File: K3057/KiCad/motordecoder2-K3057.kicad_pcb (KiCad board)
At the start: 2 copper layers, 69 x 14 mm, 85 parts, among them J11 PAD, J12 PAD, J14 PAD, J16 PAD, J18 PAD, J19 PAD, P10 PAD, P11 PAD, P21 PAD, P22 PAD, P23 PAD, P24 PAD, P25 PAD, P26 PAD, P27 PAD, P28 PAD, P29 PAD, P31 PAD, P7 PAD, P8 PAD, P9 PROG, Q1 DMG6601LVT, Q11 SSM6N7002BFE, Q12 SSM6N7002BFE, Q13 SSM6N7002BFE, Q14 SSM6N7002BFE, Q15 SSM3K7002BFU, Q2 DMG6601LVT, Q21 PMBT3906VS, Q22 SSM6N7002BFE, Q3 PMBT3904VS, Q5 2SC4116, Q6 PMBT3906VS, Q8 PMBT3904VS, U2 ATtiny1606-M

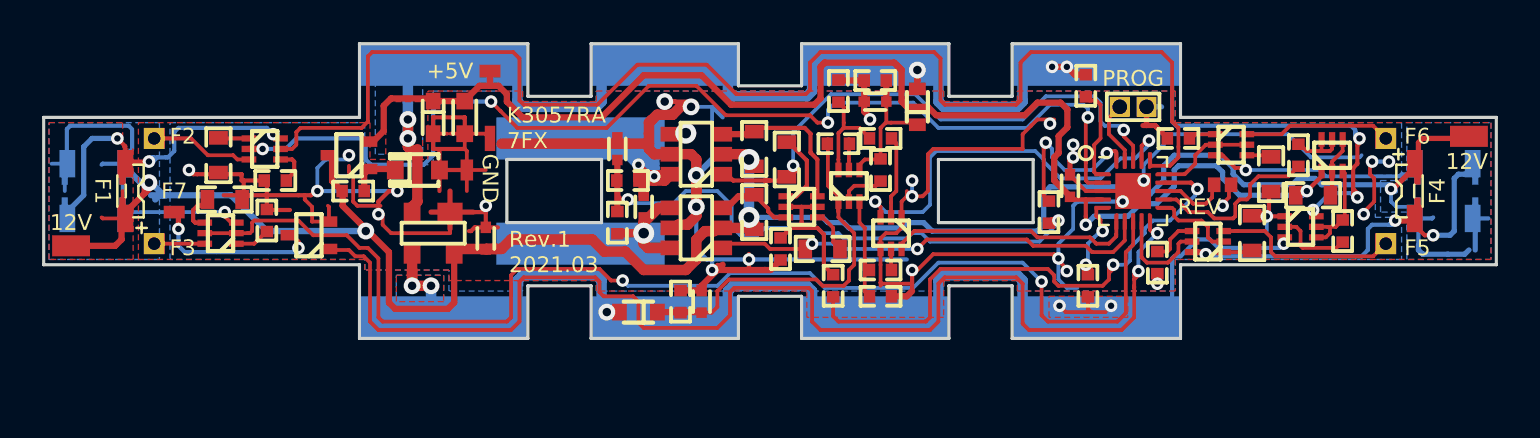
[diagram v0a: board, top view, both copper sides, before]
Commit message: 回路の問題点を修正 (K3066: Rev3 / それ以外: Rev2)
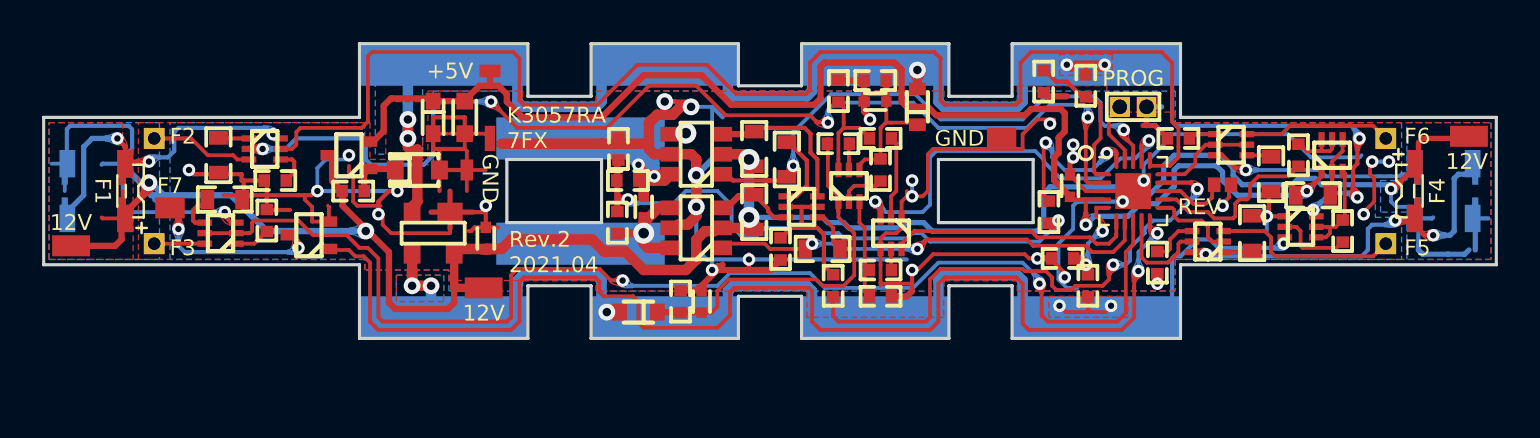
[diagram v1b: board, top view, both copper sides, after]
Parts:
- removed C6: 104, footprint:C_1005_v2
- added J13: PAD, footprint:PAD_1.0x1.8_SMD, F.Cu at (120.4, 91.6)
- added P12: PAD, footprint:PAD_1.0x1.4_SMD, F.Cu at (145.0, 84.5)
- added R16: 103, footprint:R_1005, F.Cu at (126.8, 85.0)
- added R17: 104, footprint:R_1005, F.Cu at (147.0, 81.8)
- added R18: 104, footprint:R_1005, F.Cu at (147.9, 90.2)
- C7: value 104 -> 182
- J19: footprint footprint:PAD_0.6x1.0_SMD -> footprint:PAD_1.0x1.4_SMD
- R23, R24, R25, R26: value 102 -> 472
- moved J19 0.28 mm to (105.5, 87.8)
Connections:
- net Func8 renamed DIR_JP
- Q11 pad 5: Func6 -> Func2
- Q12 pad 2: Func2 -> Func4
- Q12 pad 5: Func3 -> Func5
- Q13 pad 2: Func4 -> Func3
- Q13 pad 5: Func4 -> Func3
- Q14 pad 2: Func5 -> Func6
- Q14 pad 5: Func5 -> Func6
- U2 pad 11: Func2 -> Func4
- U2 pad 15: Func5 -> Func6
- U2 pad 16: Func6 -> Func2
- U2 pad 8: Func4 -> Func3
- U2 pad 9: Func3 -> Func5
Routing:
- net Func2: track 3.98 -> 62.9 mm
- net Func6: track 62.9 -> 4.76 mm
- net Func4: track 58.3 -> 3.98 mm, vias 2 -> 0
- net Func3: track 4.85 -> 58.1 mm, vias 0 -> 2
- net Net-(R1-Pad2): track 4.62 -> 7.14 mm
- net +12V: track 122.6 -> 124.1 mm
- net RAIL+: track 70.3 -> 71.5 mm
- net GND: track 168.9 -> 170.1 mm
- net Net-(R18-Pad1): track 4.06 -> 4.76 mm
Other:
- board text added: "Rev.2 2021.04"
- board text removed: "Rev.1 2021.03"

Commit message: 基板上のF表記をP表記に変更
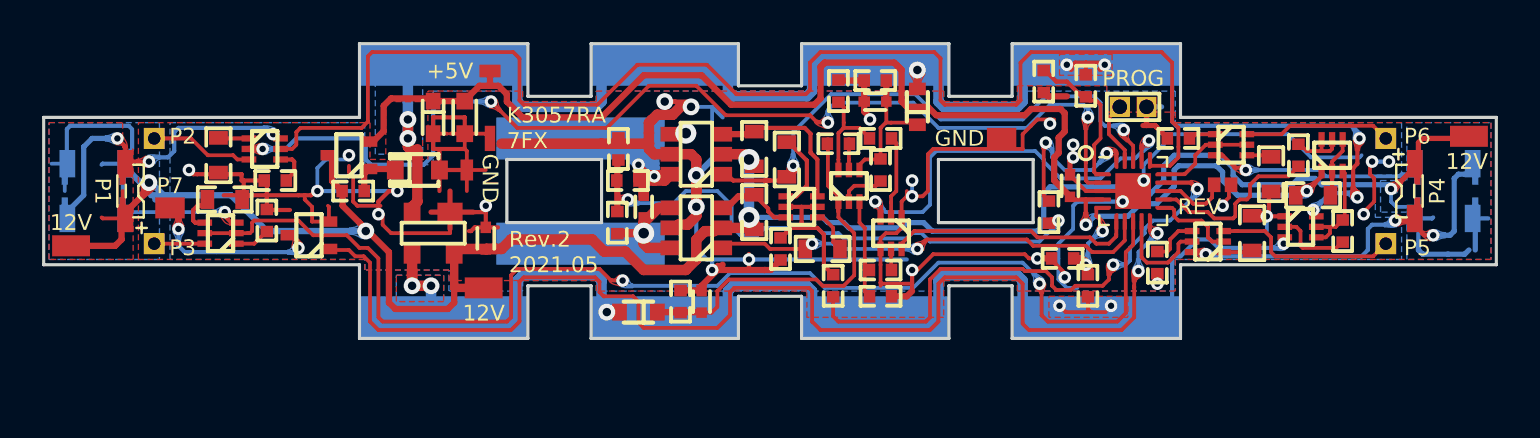
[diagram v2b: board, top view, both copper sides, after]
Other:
- board text added: "P1"
- board text added: "P1/P4"
- board text added: "P2"
- board text added: "P2/P5"
- board text added: "P3"
- board text added: "P4"
- board text added: "P5"
- board text added: "P6"
- board text added: "P7"
- board text added: "Rev.2 2021.05"
- board text removed: "F1"
- board text removed: "F1/F4"
- board text removed: "F2"
- board text removed: "F2/F5"
- board text removed: "F3"
- board text removed: "F4"
- board text removed: "F5"
- board text removed: "F6"
- board text removed: "F7"
- board text removed: "Rev.2 2021.04"
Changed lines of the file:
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@@
     (effects (font (size 0.75 0.75) (thickness 0.18)) (justify mirror))
   )
-  (gr_text "Rev.2\n2021.04" (at 121.6 89.9) (layer F.SilkS)
+  (gr_text "Rev.2\n2021.05" (at 121.6 89.9) (layer F.SilkS)
     (effects (font (size 0.75 0.75) (thickness 0.18)) (justify left))
   )
-  (gr_text F2 (at 106.1 84.3 180) (layer B.SilkS)
+  (gr_text P2 (at 106.1 84.3 180) (layer B.SilkS)
     (effects (font (size 0.75 0.75) (thickness 0.18)) (justify mirror))
   )
@@
     (effects (font (size 0.75 0.75) (thickness 0.18)))
   )
-  (gr_text F7 (at 105.5 86.75) (layer F.SilkS)
+  (gr_text P7 (at 105.5 86.75) (layer F.SilkS)
     (effects (font (size 0.75 0.75) (thickness 0.18)))
   )
@@
     (effects (font (size 0.75 0.75) (thickness 0.18)))
   )
-  (gr_text F3 (at 103.5 89.7 -90) (layer B.SilkS)
+  (gr_text P3 (at 103.5 89.7 -90) (layer B.SilkS)
     (effects (font (size 0.75 0.75) (thickness 0.18)) (justify mirror))
   )
-  (gr_text F1 (at 100.8 89.7 270) (layer B.SilkS)
+  (gr_text P1 (at 100.8 89.7 270) (layer B.SilkS)
     (effects (font (size 0.75 0.75) (thickness 0.18)) (justify mirror))
   )
-  (gr_text F3 (at 106.1 89.7) (layer F.SilkS)
+  (gr_text P3 (at 106.1 89.7) (layer F.SilkS)
     (effects (font (size 0.75 0.75) (thickness 0.18)))
   )
-  (gr_text F2 (at 106.1 84.4) (layer F.SilkS)
+  (gr_text P2 (at 106.1 84.4) (layer F.SilkS)
     (effects (font (size 0.75 0.75) (thickness 0.18)))
   )
-  (gr_text F1 (at 102.3 87 -90) (layer F.SilkS)
+  (gr_text P1 (at 102.3 87 -90) (layer F.SilkS)
     (effects (font (size 0.75 0.75) (thickness 0.18)))
   )
@@
     (effects (font (size 0.75 0.75) (thickness 0.18)))
   )
-  (gr_text F4 (at 167.25 84.25 90) (layer B.SilkS)
+  (gr_text P4 (at 167.25 84.25 90) (layer B.SilkS)
     (effects (font (size 0.75 0.75) (thickness 0.18)) (justify mirror))
   )
@@
     (effects (font (size 0.75 0.75) (thickness 0.18)))
   )
-  (gr_text F5 (at 161.75 89.7 180) (layer B.SilkS)
+  (gr_text P5 (at 161.75 89.7 180) (layer B.SilkS)
     (effects (font (size 0.75 0.75) (thickness 0.18)) (justify mirror))
   )
-  (gr_text F6 (at 164.75 84.25 90) (layer B.SilkS)
+  (gr_text P6 (at 164.75 84.25 90) (layer B.SilkS)
     (effects (font (size 0.75 0.75) (thickness 0.18)) (justify mirror))
   )
-  (gr_text F4 (at 165.7 87 90) (layer F.SilkS)
+  (gr_text P4 (at 165.7 87 90) (layer F.SilkS)
     (effects (font (size 0.75 0.75) (thickness 0.18)))
   )
-  (gr_text F5 (at 164.75 89.7) (layer F.SilkS)
+  (gr_text P5 (at 164.75 89.7) (layer F.SilkS)
     (effects (font (size 0.75 0.75) (thickness 0.18)))
   )
-  (gr_text F6 (at 164.75 84.4) (layer F.SilkS)
+  (gr_text P6 (at 164.75 84.4) (layer F.SilkS)
     (effects (font (size 0.75 0.75) (thickness 0.18)))
   )
@@
     (arrow2b (pts (xy 168.5 101.5) (xy 167.373496 102.086421)))
   )
-  (gr_text F2/F5 (at 171.2 87.2) (layer Eco2.User)
+  (gr_text P2/P5 (at 171.2 87.2) (layer Eco2.User)
     (effects (font (size 1 1) (thickness 0.15)))
   )
-  (gr_text F1/F4 (at 96.6 87) (layer Eco2.User)
+  (gr_text P1/P4 (at 96.6 87) (layer Eco2.User)
     (effects (font (size 1 1) (thickness 0.15)))
   )
-  (gr_text F4 (at 98 89.5) (layer Eco2.User)
+  (gr_text P4 (at 98 89.5) (layer Eco2.User)
     (effects (font (size 1 1) (thickness 0.15)))
   )
-  (gr_text F6 (at 98 84.5) (layer Eco2.User)
+  (gr_text P6 (at 98 84.5) (layer Eco2.User)
     (effects (font (size 1 1) (thickness 0.15)))
   )
-  (gr_text F5 (at 169.75 84.5) (layer Eco2.User)
+  (gr_text P5 (at 169.75 84.5) (layer Eco2.User)
     (effects (font (size 1 1) (thickness 0.15)))
   )
-  (gr_text F3 (at 169.75 89.75) (layer Eco2.User)
+  (gr_text P3 (at 169.75 89.75) (layer Eco2.User)
     (effects (font (size 1 1) (thickness 0.15)))
   )

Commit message: (K3057RA) 表面のLEDパッドを増設
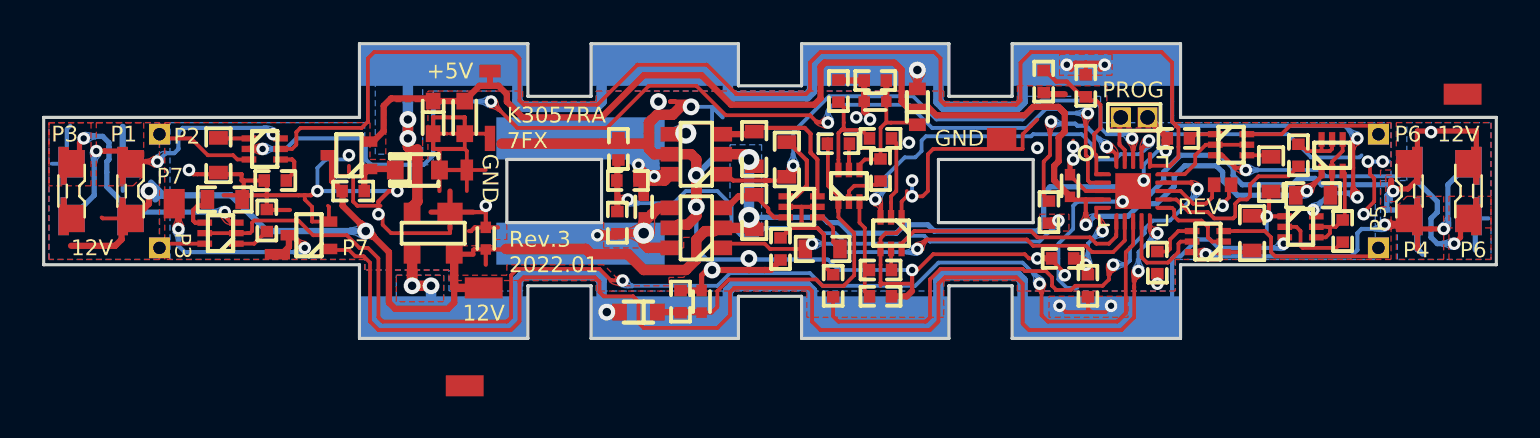
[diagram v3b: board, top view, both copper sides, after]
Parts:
- added D17: LED, footprint:LED_1224_1005_SIDE_BIG2, F.Cu at (167.8, 87.0)
- added D18: LED, footprint:LED_1224_1005_SIDE_BIG2, F.Cu at (100.2, 87.0)
- added J20: PAD, footprint:PAD_0.5x1.2_SMD, F.Cu at (110.6, 90.0)
- D11, D12, D13, D14, D15, D16: footprint footprint:LED_1224_1005_SIDE -> footprint:LED_1224_1005_SIDE_BIG2
- moved P7 19.7 mm to (120.4, 91.6), turned to 270 degrees
- moved J13 4.74 mm to (119.5, 96.2)
- moved J11 2.02 mm to (166.9, 82.4)
- moved P9 0.50 mm to (151.3, 83.5)
- moved J12 0.40 mm to (162.9, 89.7)
- moved J16 0.40 mm to (162.9, 84.3)
- moved J14 0.32 mm to (105.0, 89.7)
- moved J18 0.32 mm to (105.0, 84.3)
- moved J19 0.28 mm to (105.7, 87.6), turned to 180 degrees
- moved D14 0.05 mm to (167.8, 87.0)
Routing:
- net Net-(D15-Pad1): track 10.8 -> 19.7 mm, vias 1 -> 2
- net Net-(D16-Pad1): track 6.53 -> 12.6 mm, vias 1 -> 2
- net Net-(D12-Pad1): track 20.2 -> 22.1 mm
- net Net-(J19-Pad1): track 8.46 -> 10.1 mm
- net GND: track 170.1 -> 168.6 mm, vias 29 -> 32
- net Net-(D11-Pad1): track 17.6 -> 16.2 mm
- net +12V: track 124.1 -> 122.7 mm, vias 5 -> 6
- net MOTOR-: track 5.23 -> 6.21 mm, vias 1 -> 2
- net ABC-: track 19.1 -> 18.2 mm
- net UPDI: track 3.07 -> 2.26 mm
- net RAIL+: track 71.5 -> 70.8 mm
- net Func1: track 51.9 -> 51.3 mm
- net BEMF: track 8.58 -> 8.07 mm
- added copper zone on F.Cu, net Net-(D11-Pad1)
- added copper zone on F.Cu, net Net-(D12-Pad1)
- added copper zone on F.Cu, net Net-(D15-Pad1)
- added copper zone on F.Cu, net Net-(D16-Pad1)
- added copper zone on F.Cu, net Net-(R10-Pad1)
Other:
- board text added: "<- FWD"
- board text added: "K3057RA"
- board text added: "REV ->"
- board text added: "Rev.3 2022.01"
- board text removed: "Rev.2 2021.05"
